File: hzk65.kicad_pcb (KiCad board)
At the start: 2 copper layers, 314.3 x 100 mm, 136 parts, among them SW1 SW_Push, SW10 SW_Push, SW11 SW_Push, SW12 SW_Push, SW13 SW_Push, SW14 SW_Push, SW16 SW_Push, SW17 SW_Push, SW18 SW_Push, SW19 SW_Push, SW2 SW_Push, SW20 SW_Push, SW21 SW_Push, SW22 SW_Push, SW23 SW_Push, SW24 SW_Push, SW25 SW_Push, SW26 SW_Push, SW27 SW_Push, SW28 SW_Push, SW29 SW_Push, SW3 SW_Push, SW31 SW_Push, SW32 SW_Push, SW33 SW_Push, SW34 SW_Push, SW35 SW_Push, SW36 SW_Push, SW37 SW_Push, SW38 SW_Push, SW39 SW_Push, SW4 SW_Push, SW40 SW_Push, SW41 SW_Push, SW42 SW_Push, SW44 SW_Push, SW46 SW_Push, SW48 SW_Push, SW49 SW_Push, SW5 SW_Push, SW50 SW_Push, SW51 SW_Push, SW52 SW_Push, SW53 SW_Push, SW54 SW_Push, SW55 SW_Push, SW56 SW_Push, SW57 SW_Push, SW58 SW_Push, SW59 SW_Push, SW6 SW_Push, SW60 SW_Push, SW61 SW_Push, SW62 SW_Push, SW63 SW_Push, SW67 SW_Push, SW7 SW_Push, SW70 SW_Push, SW71 SW_Push, SW72 SW_Push, SW73 SW_Push, SW74 SW_Push, SW75 SW_Push, SW8 SW_Push, SW9 SW_Push

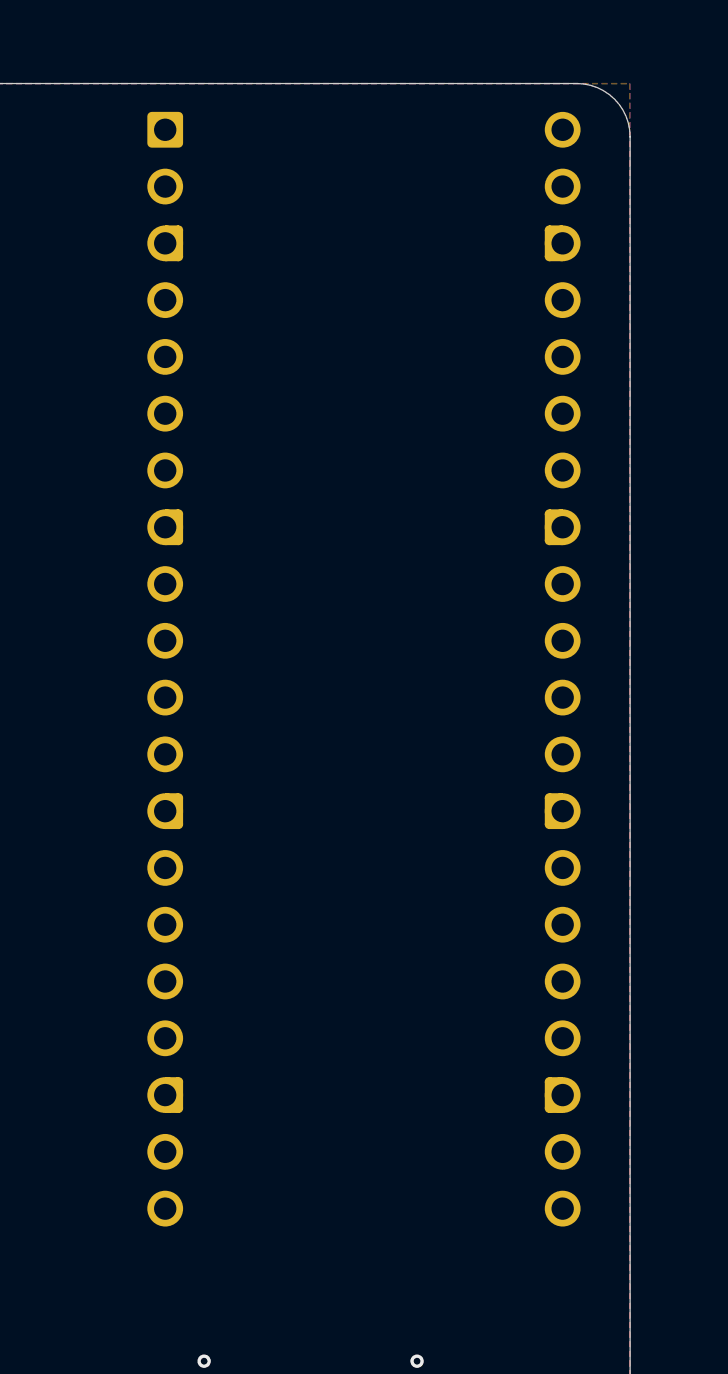
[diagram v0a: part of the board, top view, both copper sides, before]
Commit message: Add temporary socket connectors for plate
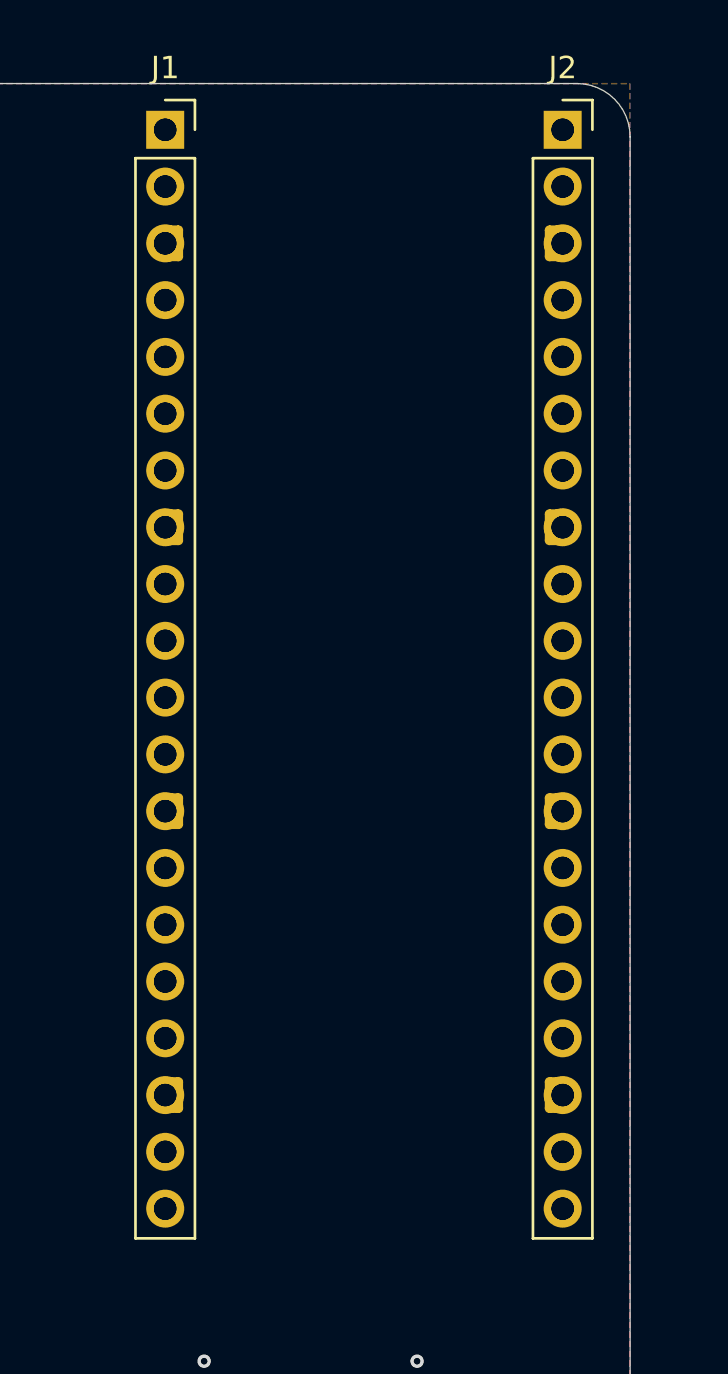
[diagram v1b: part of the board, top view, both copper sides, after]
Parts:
- added J1: PinSocket_1x20_P2.54mm_Vertical, Connector_PinSocket_2.54mm:PinSocket_1x20_P2.54mm_Vertical, F.Cu at (345.9, 102.1)
- added J2: PinSocket_1x20_P2.54mm_Vertical, Connector_PinSocket_2.54mm:PinSocket_1x20_P2.54mm_Vertical, F.Cu at (363.7, 102.1)

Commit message: Update switch plate with new cutout
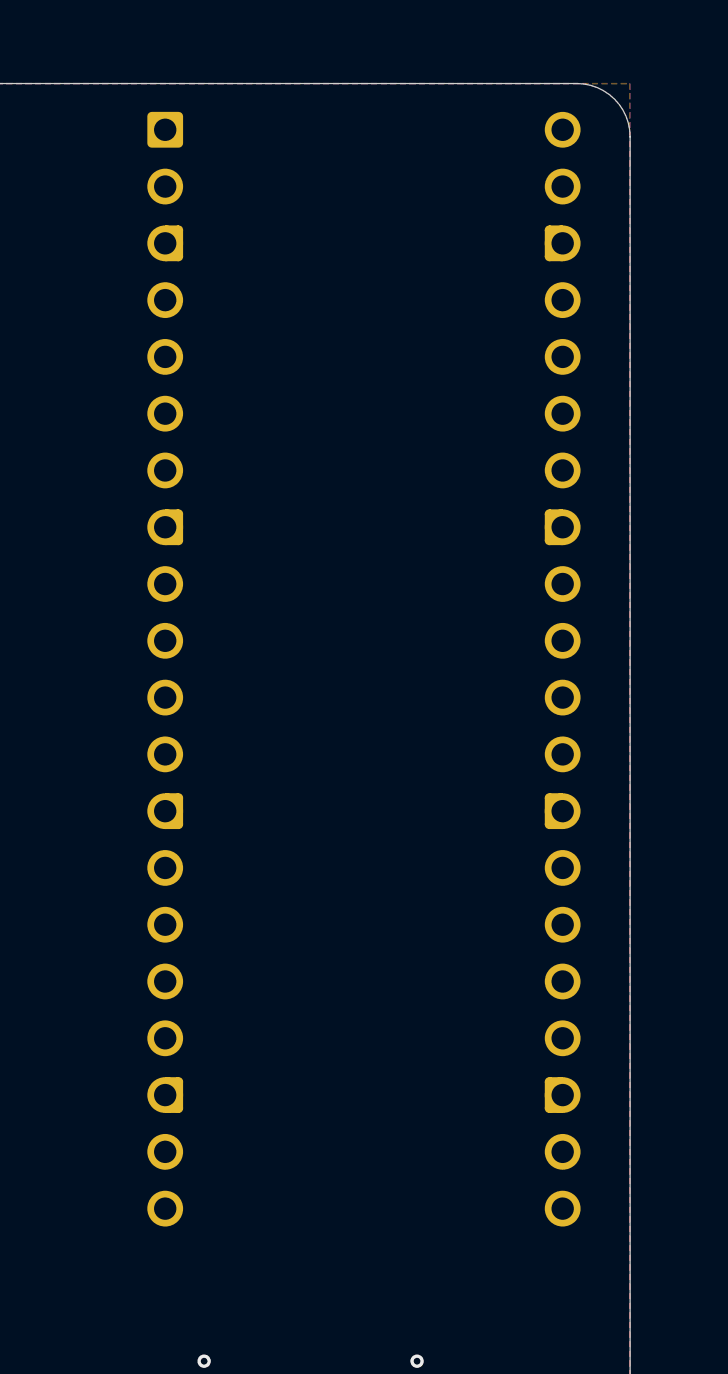
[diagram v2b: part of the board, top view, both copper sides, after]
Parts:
- removed J1, J2: PinSocket_1x20_P2.54mm_Vertical, Connector_PinSocket_2.54mm:PinSocket_1x20_P2.54mm_Vertical
